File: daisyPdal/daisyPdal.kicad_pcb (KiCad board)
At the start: 2 copper layers, 76 x 80 mm, 39 parts, among them J1 Guitar in, J2 Left out, J3 fsw pin 1, J4 fsw pin 4, J5 fsw pin 6, J6 fsw pin 3, J7 fsw pin 2, J8 fsw pin 5, SW1 Switch 1, SW2 Switch 2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

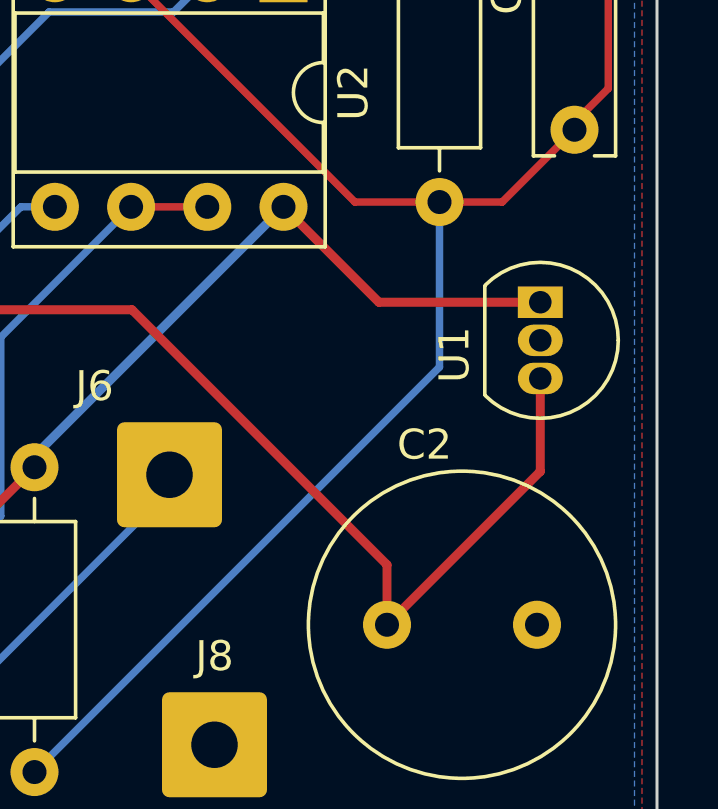
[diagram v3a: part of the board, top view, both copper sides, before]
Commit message: Replace u1 footprint to get correct spacing
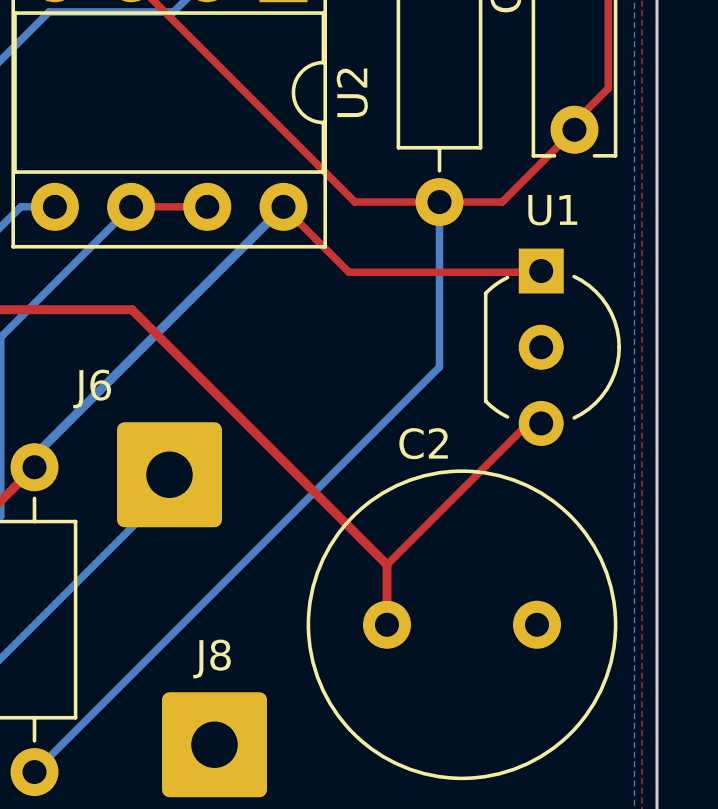
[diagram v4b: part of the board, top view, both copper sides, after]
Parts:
- U1: footprint Package_TO_SOT_THT:TO-92_Inline -> Package_TO_SOT_THT:TO-92_Inline_Wide
- moved U1 1.04 mm to (172.1, 101.0)
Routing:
- net /VCC: track 144.8 -> 141.6 mm
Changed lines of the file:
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@@
     )
   )
-  (footprint "Package_TO_SOT_THT:TO-92_Inline" (layer "F.Cu")
-    (at 172.11 102 -90)
-    (descr "TO-92 leads in-line, narrow, oval pads, drill 0.75mm (see NXP sot054_po.pdf)")
+  (footprint "Package_TO_SOT_THT:TO-92_Inline_Wide" (layer "F.Cu")
+    (at 172.14 100.96 -90)
+    (descr "TO-92 leads in-line, wide, drill 0.75mm (see NXP sot054_po.pdf)")
     (tags "to-92 sc-43 sc-43a sot54 PA33 transistor")
     (property "Sheetfile" "daisyPdal.kicad_sch")
@@
     (property "ki_keywords" "Voltage Regulator 100mA Positive")
     (attr through_hole)
-    (fp_text reference "U1" (at 1.75 2.86 90) (layer "F.SilkS")
-        (effects (font (size 1 1) (thickness 0.15)))
-    )
-    (fp_text value "L78L05_TO92" (at -0.23 2.79 90) (layer "F.Fab")
-        (effects (font (size 1 1) (thickness 0.15)))
-    )
-    (fp_text user "${REFERENCE}" (at 7.62 -5.08 90) (layer "F.Fab")
-        (effects (font (size 1 1) (thickness 0.15)))
-    )
-    (fp_line (start -0.53 1.85) (end 3.07 1.85)
-      (stroke (width 0.12) (type solid)) (layer "F.SilkS"))
-    (fp_arc (start -0.568478 1.838478) (mid -1.132087 -0.994977) (end 1.27 -2.6)
-      (stroke (width 0.12) (type solid)) (layer "F.SilkS"))
-    (fp_arc (start 1.27 -2.6) (mid 3.672087 -0.994977) (end 3.108478 1.838478)
-      (stroke (width 0.12) (type solid)) (layer "F.SilkS"))
-    (fp_line (start -1.46 -2.73) (end -1.46 2.01)
-      (stroke (width 0.05) (type solid)) (layer "F.CrtYd"))
-    (fp_line (start -1.46 -2.73) (end 4 -2.73)
-      (stroke (width 0.05) (type solid)) (layer "F.CrtYd"))
-    (fp_line (start 4 2.01) (end -1.46 2.01)
-      (stroke (width 0.05) (type solid)) (layer "F.CrtYd"))
-    (fp_line (start 4 2.01) (end 4 -2.73)
-      (stroke (width 0.05) (type solid)) (layer "F.CrtYd"))
-    (fp_line (start -0.5 1.75) (end 3 1.75)
-      (stroke (width 0.1) (type solid)) (layer "F.Fab"))
-    (fp_arc (start -0.483625 1.753625) (mid -1.021221 -0.949055) (end 1.27 -2.48)
-      (stroke (width 0.1) (type solid)) (layer "F.Fab"))
-    (fp_arc (start 1.27 -2.48) (mid 3.561221 -0.949055) (end 3.023625 1.753625)
-      (stroke (width 0.1) (type solid)) (layer "F.Fab"))
-    (pad "1" thru_hole rect (at 0 0 270) (size 1.05 1.5) (drill 0.75) (layers "*.Cu" "*.Mask")
+    (fp_text reference "U1" (at -2 -0.39) (layer "F.SilkS")
+        (effects (font (size 1 1) (thickness 0.15)))
+    )
+    (fp_text value "L78L05_TO92" (at 2.54 2.79 -90) (layer "F.Fab")
+        (effects (font (size 1 1) (thickness 0.15)))
+    )
+    (fp_text user "${REFERENCE}" (at 2.54 0 -90) (layer "F.Fab")
+        (effects (font (size 1 1) (thickness 0.15)))
+    )
+    (fp_line (start 0.74 1.85) (end 4.34 1.85)
+      (stroke (width 0.12) (type solid)) (layer "F.SilkS"))
+    (fp_arc (start 0.1836 -1.098807) (mid 1.143021 -2.192817) (end 2.54 -2.6)
+      (stroke (width 0.12) (type solid)) (layer "F.SilkS"))
+    (fp_arc (start 0.74 1.85) (mid 0.446097 1.509328) (end 0.215816 1.122795)
+      (stroke (width 0.12) (type solid)) (layer "F.SilkS"))
+    (fp_arc (start 2.54 -2.6) (mid 3.936979 -2.192818) (end 4.8964 -1.098807)
+      (stroke (width 0.12) (type solid)) (layer "F.SilkS"))
+    (fp_arc (start 4.864184 1.122795) (mid 4.633903 1.509328) (end 4.34 1.85)
+      (stroke (width 0.12) (type solid)) (layer "F.SilkS"))
+    (fp_line (start -1.01 -2.73) (end -1.01 2.01)
+      (stroke (width 0.05) (type solid)) (layer "F.CrtYd"))
+    (fp_line (start -1.01 -2.73) (end 6.09 -2.73)
+      (stroke (width 0.05) (type solid)) (layer "F.CrtYd"))
+    (fp_line (start 6.09 2.01) (end -1.01 2.01)
+      (stroke (width 0.05) (type solid)) (layer "F.CrtYd"))
+    (fp_line (start 6.09 2.01) (end 6.09 -2.73)
+      (stroke (width 0.05) (type solid)) (layer "F.CrtYd"))
+    (fp_line (start 0.8 1.75) (end 4.3 1.75)
+      (stroke (width 0.1) (type solid)) (layer "F.Fab"))
+    (fp_arc (start 0.786375 1.753625) (mid 0.248779 -0.949055) (end 2.54 -2.48)
+      (stroke (width 0.1) (type solid)) (layer "F.Fab"))
+    (fp_arc (start 2.54 -2.48) (mid 4.831221 -0.949055) (end 4.293625 1.753625)
+      (stroke (width 0.1) (type solid)) (layer "F.Fab"))
+    (pad "1" thru_hole rect (at 0 0 270) (size 1.5 1.5) (drill 0.8) (layers "*.Cu" "*.Mask")
       (net 41 "+5V") (pinfunction "VO") (pintype "power_out"))
-    (pad "2" thru_hole oval (at 1.27 0 270) (size 1.05 1.5) (drill 0.75) (layers "*.Cu" "*.Mask")
+    (pad "2" thru_hole circle (at 2.54 0 270) (size 1.5 1.5) (drill 0.8) (layers "*.Cu" "*.Mask")
       (net 20 "GND") (pinfunction "GND") (pintype "power_in"))
-    (pad "3" thru_hole oval (at 2.54 0 270) (size 1.05 1.5) (drill 0.75) (layers "*.Cu" "*.Mask")
+    (pad "3" thru_hole circle (at 5.08 0 270) (size 1.5 1.5) (drill 0.8) (layers "*.Cu" "*.Mask")
       (net 39 "/VCC") (pinfunction "VI") (pintype "power_in"))
-    (model "${KICAD6_3DMODEL_DIR}/Package_TO_SOT_THT.3dshapes/TO-92_Inline.wrl"
+    (model "${KICAD6_3DMODEL_DIR}/Package_TO_SOT_THT.3dshapes/TO-92_Inline_Wide.wrl"
       (offset (xyz 0 0 0))
       (scale (xyz 1 1 1))
@@
   (segment (start 145.044154 86) (end 143.519154 84.475) (width 0.25) (layer "F.Cu") (net 35))
   (segment (start 122.945 84.475) (end 114.92 92.5) (width 0.25) (layer "F.Cu") (net 35))
+  (segment (start 171.71 106.04) (end 167 110.75) (width 0.25) (layer "F.Cu") (net 39))
   (segment (start 102.75 90.49) (end 102.75 83.75) (width 0.3) (layer "F.Cu") (net 39))
   (segment (start 104.76 92.5) (end 104.76 94.51) (width 0.3) (layer "F.Cu") (net 39))
-  (segment (start 172.11 107.64) (end 167 112.75) (width 0.3) (layer "F.Cu") (net 39))
   (segment (start 109.583704 51.1) (end 105.85 54.833704) (width 0.3) (layer "F.Cu") (net 39))
   (segment (start 112.5 102.25) (end 158.5 102.25) (width 0.3) (layer "F.Cu") (net 39))
   (segment (start 102.75 83.75) (end 102.75 79.5) (width 0.3) (layer "F.Cu") (net 39))
   (segment (start 158.5 102.25) (end 167 110.75) (width 0.3) (layer "F.Cu") (net 39))
+  (segment (start 172.14 106.04) (end 171.71 106.04) (width 0.25) (layer "F.Cu") (net 39))
   (segment (start 102.75 79.5) (end 106 76.25) (width 0.3) (layer "F.Cu") (net 39))
   (segment (start 124.46 51.1) (end 109.583704 51.1) (width 0.3) (layer "F.Cu") (net 39))
   (segment (start 104.76 94.51) (end 112.5 102.25) (width 0.3) (layer "F.Cu") (net 39))
   (segment (start 125.5 50.06) (end 124.46 51.1) (width 0.3) (layer "F.Cu") (net 39))
-  (segment (start 172.11 104.54) (end 172.11 107.64) (width 0.3) (layer "F.Cu") (net 39))
   (segment (start 167 110.75) (end 167 112.75) (width 0.3) (layer "F.Cu") (net 39))
   (segment (start 104.76 92.5) (end 102.75 90.49) (width 0.3) (layer "F.Cu") (net 39))
@@
   (segment (start 125.5 42.44) (end 130.44 42.44) (width 0.3) (layer "F.Cu") (net 40))
   (segment (start 116.07 111.35) (end 151.4 111.35) (width 0.3) (layer "F.Cu") (net 41))
+  (segment (start 165.73 101) (end 163.55 98.82) (width 0.25) (layer "F.Cu") (net 41))
   (segment (start 114.67 112.75) (end 116.07 111.35) (width 0.3) (layer "F.Cu") (net 41))
   (segment (start 151.4 111.35) (end 155.25 107.5) (width 0.3) (layer "F.Cu") (net 41))
   (segment (start 110 112.75) (end 114.67 112.75) (width 0.3) (layer "F.Cu") (net 41))
-  (segment (start 166.73 102) (end 172.11 102) (width 0.3) (layer "F.Cu") (net 41))
   (segment (start 110 117) (end 110 112.75) (width 0.3) (layer "F.Cu") (net 41))
-  (segment (start 163.55 98.82) (end 166.73 102) (width 0.3) (layer "F.Cu") (net 41))
+  (segment (start 172.25 101) (end 165.73 101) (width 0.25) (layer "F.Cu") (net 41))
+  (segment (start 172.14 100.96) (end 172.21 100.96) (width 0.25) (layer "F.Cu") (net 41))
+  (segment (start 172.21 100.96) (end 172.25 101) (width 0.25) (layer "F.Cu") (net 41))
   (segment (start 155.25 107.12) (end 155.25 107.5) (width 0.3) (layer "B.Cu") (net 41))
   (segment (start 163.55 98.82) (end 155.25 107.12) (width 0.3) (layer "B.Cu") (net 41))
